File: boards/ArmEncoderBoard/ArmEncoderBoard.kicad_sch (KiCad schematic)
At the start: 5 parts, among them J1 S6B-PH-SM4-TB

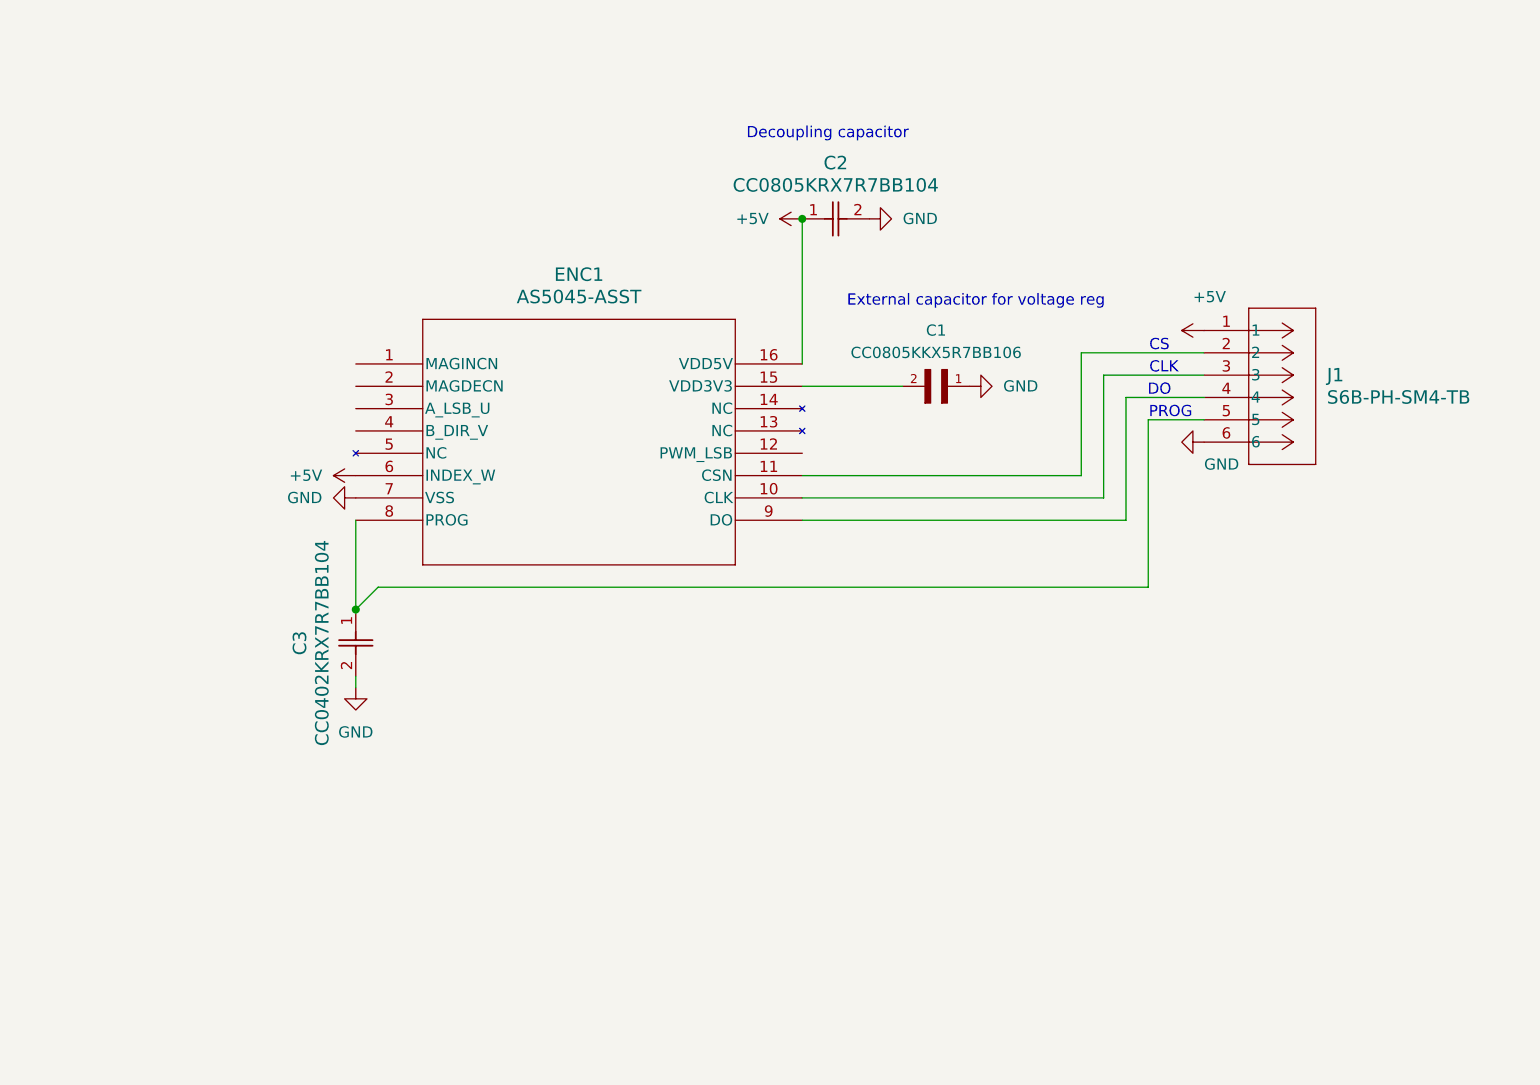
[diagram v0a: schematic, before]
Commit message: Footprints for encoder board dependencies
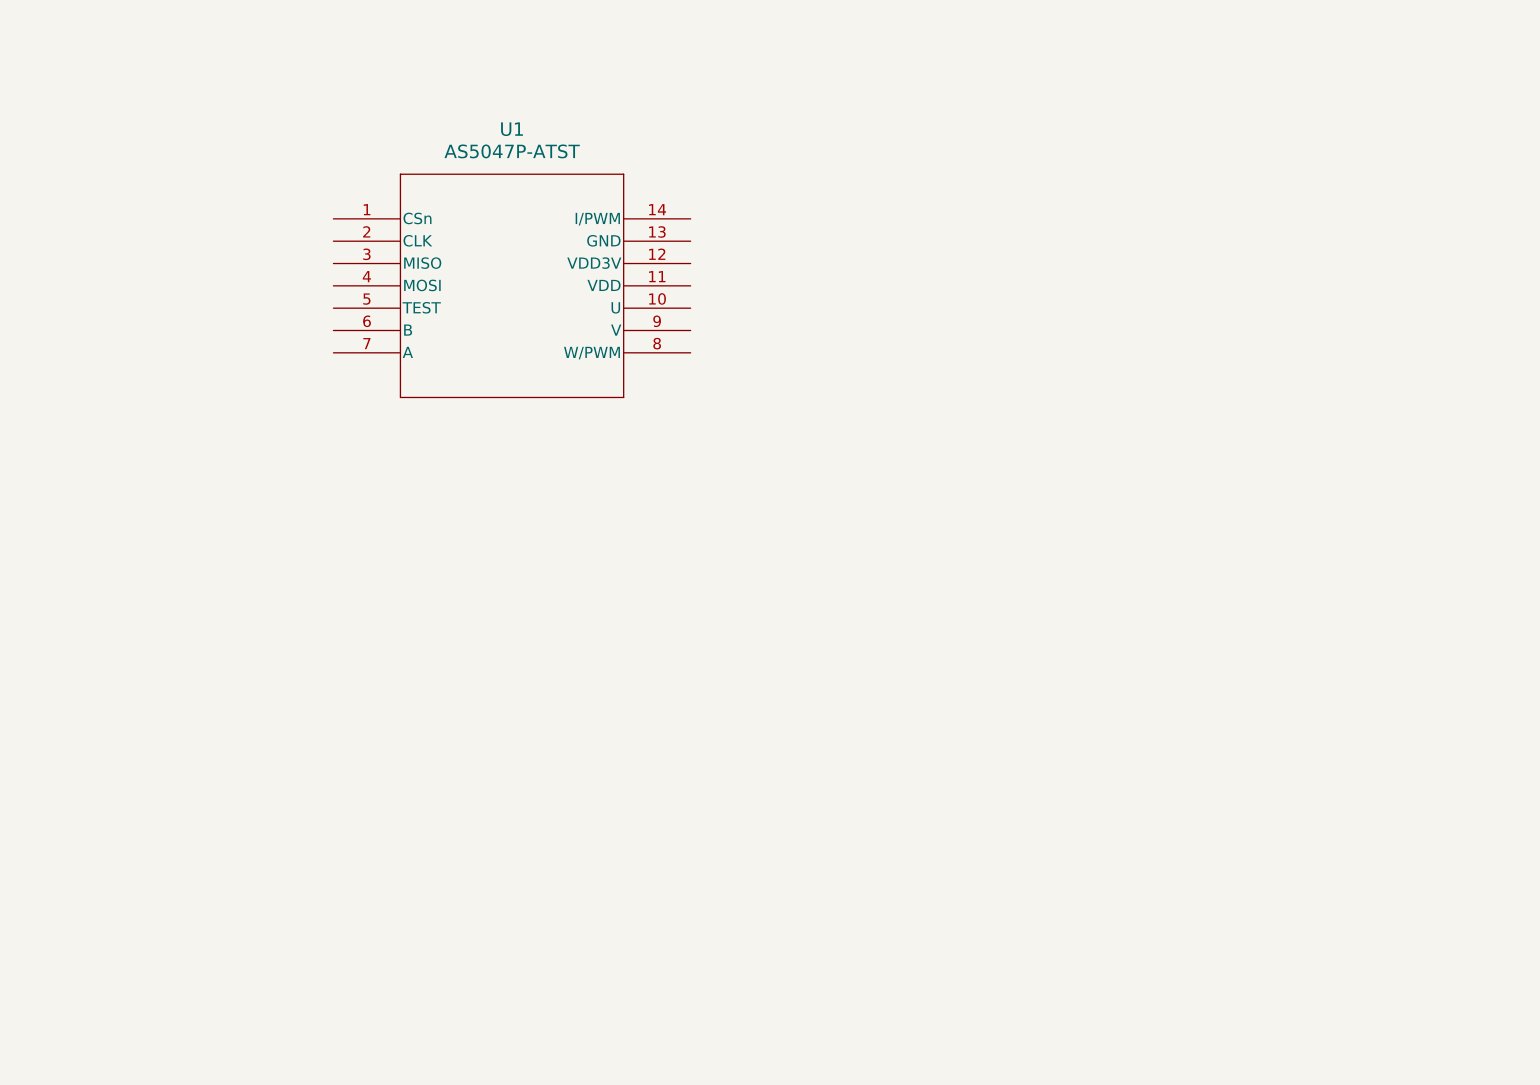
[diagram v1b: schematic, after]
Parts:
- removed C1: CC0805KKX5R7BB106, AS5045-3V3-REG-CAP:CAPC2012X70, symbol AS5045-3V-REG:CC0805KKX5R7BB106
- removed C2: CC0805KRX7R7BB104, CC0805N_YAG, symbol AS5045-DECOUPL-CAP:CC0805KRX7R7BB104
- removed C3: CC0402KRX7R7BB104, YAG_CC0402_YAG, symbol AS5045-PROG-CAP:CC0402KRX7R7BB104
- removed ENC1: AS5045-ASST, SSOP16_AS5040-ASST_AMS, symbol AS5045:AS5040-ASST
- removed J1: S6B-PH-SM4-TB, CONN_S6B-XH-SM4-TB_JST, symbol JST-XH-6:S6B-XH-SM4-TB
- added U1: AS5047P-ATST, AS5047P:AS5047P-ATST, symbol AS5047P:AS5047P-ATSM
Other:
- note removed: "CLK"
- note removed: "CS"
- note removed: "DO"
- note removed: "Decoupling capacitor"
- note removed: "External capacitor for voltage reg"
- note removed: "PROG"

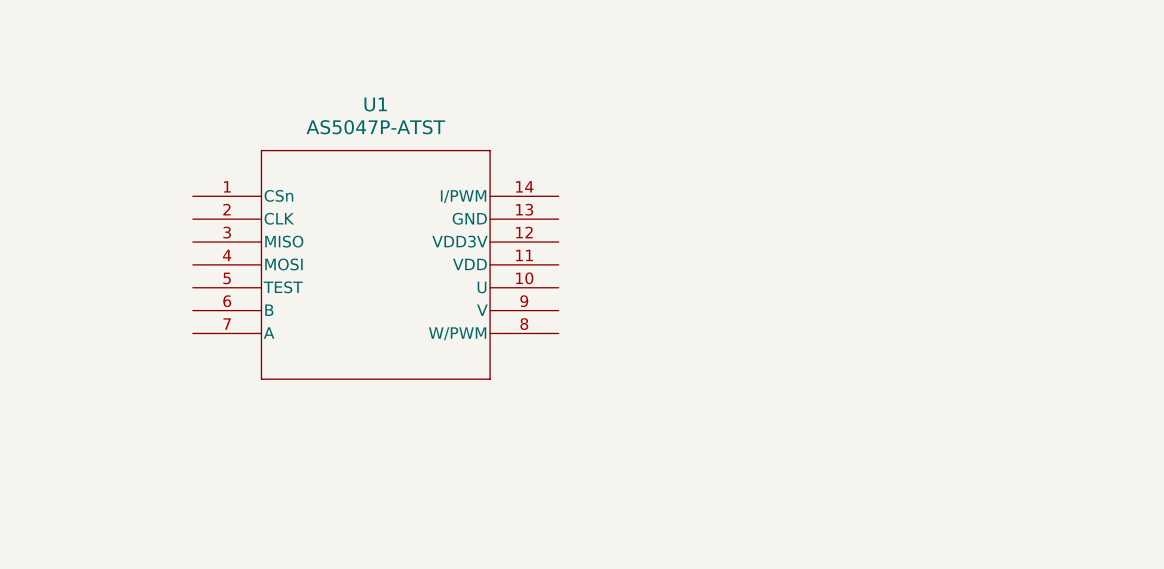
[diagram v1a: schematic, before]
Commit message: Split into leg and arm, finish arm encoder
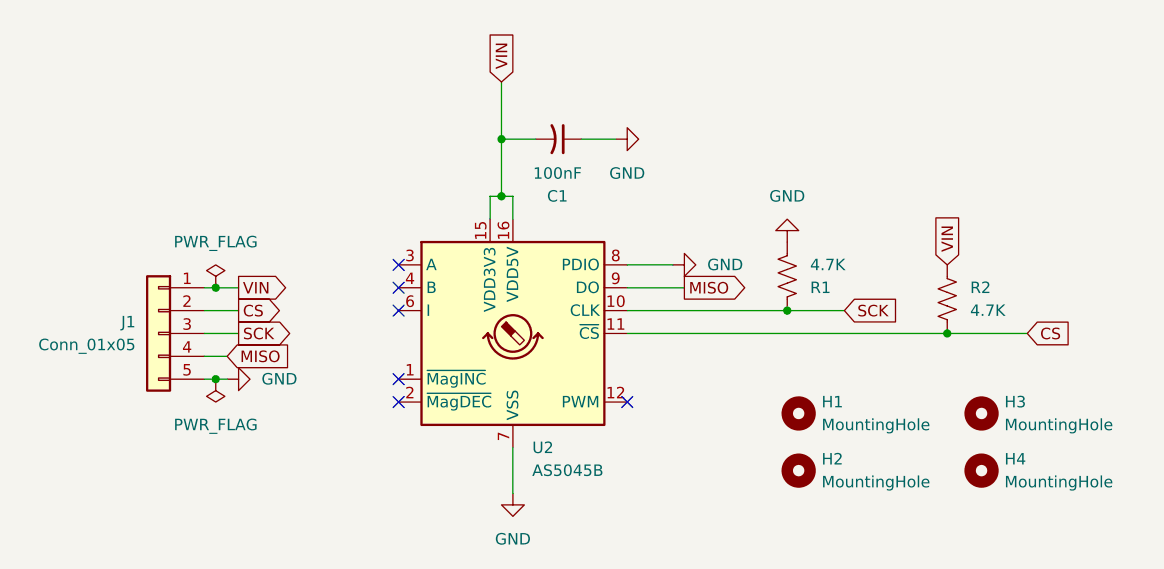
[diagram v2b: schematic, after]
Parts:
- removed U1: AS5047P-ATST, AS5047P:AS5047P-ATST, symbol AS5047P:AS5047P-ATSM
- added C1: 100nF, Capacitor100nF:885342208002, symbol Device:C_Small_US
- added H1, H2, H3, H4: MountingHole, MountingHole:MountingHole_3.5mm_Pad, symbol Mechanical:MountingHole
- added J1: Conn_01x05, Connector_JST:JST_XH_B5B-XH-A_1x05_P2.50mm_Vertical, symbol Connector_Generic:Conn_01x05
- added R1, R2: 4.7K, Resistor4.7K:CR0603-FX-4701ELF, symbol Device:R_US
- added U2: AS5045B, Package_SO:SSOP-16_5.3x6.2mm_P0.65mm, symbol Sensor_Magnetic:AS5045B
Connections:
- new net CS: J1.2 (Pin_2), R2.2, U2.11 (~{CS})
- new net GND: C1.1, J1.5 (Pin_5), R1.2, U2.7 (VSS), U2.8 (PDIO)
- new net MISO: J1.4 (Pin_4), U2.9 (DO)
- new net SCK: J1.3 (Pin_3), R1.1, U2.10 (CLK)
- new net VIN: C1.2, J1.1 (Pin_1), R2.1, U2.15 (VDD3V3), U2.16 (VDD5V)
- no-connect marks 0 -> 6
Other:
- title: Upper Arm Encoder Board -> Arm Encoder Board

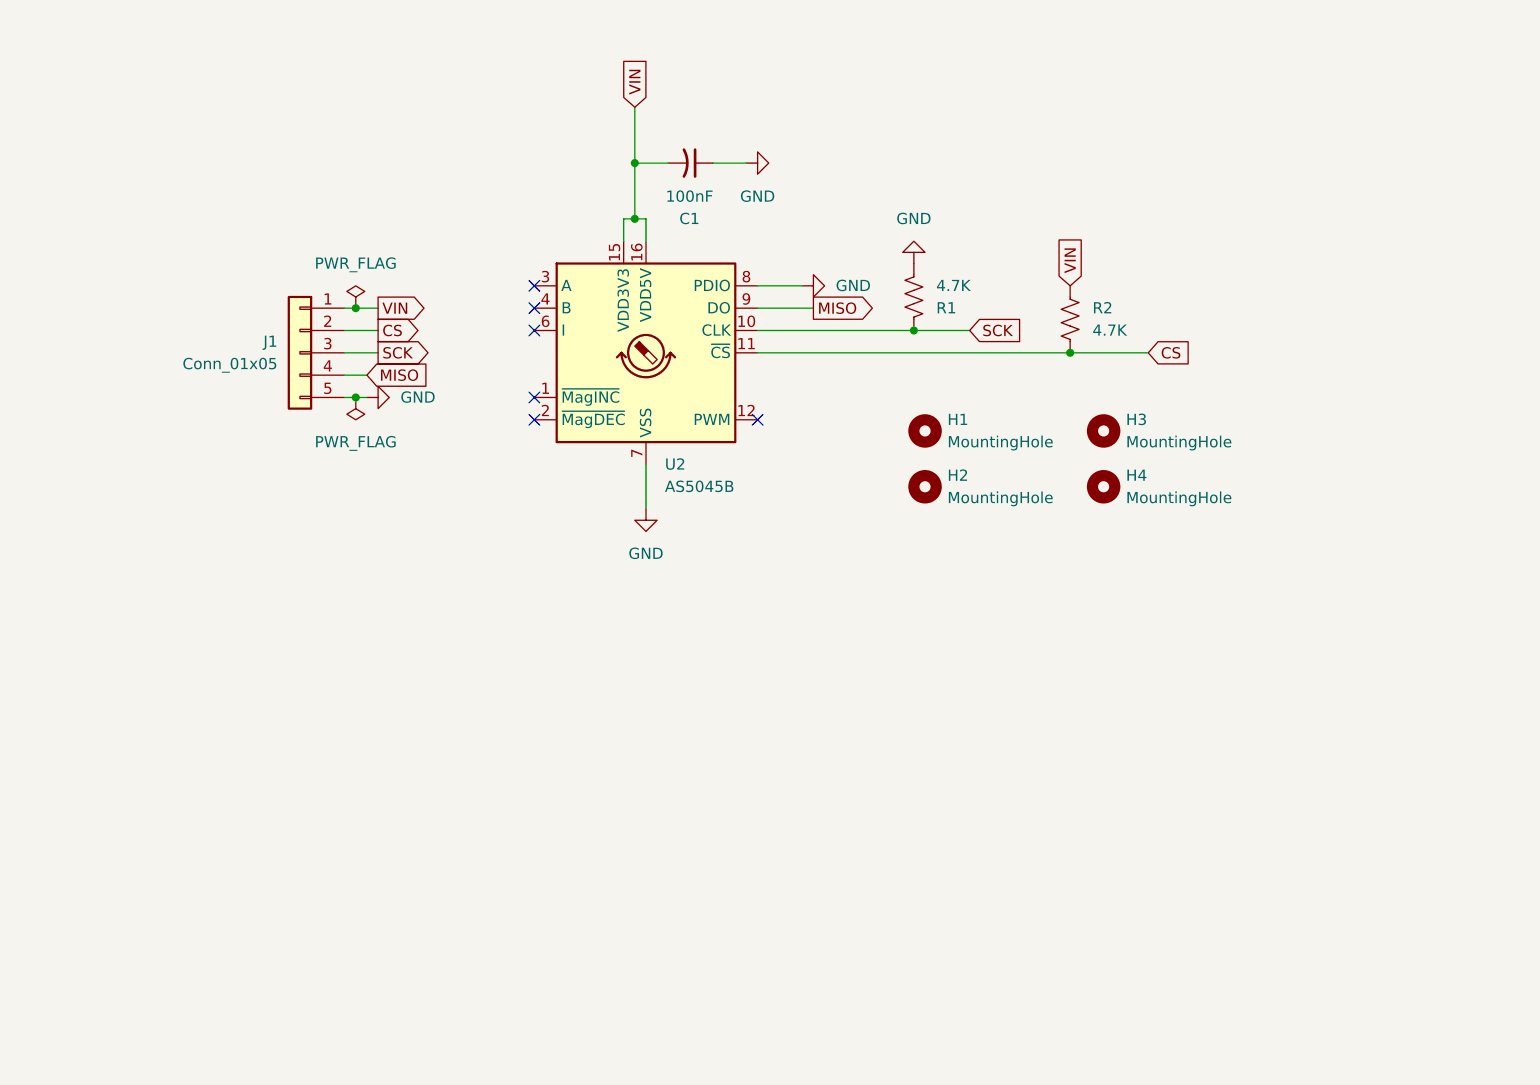
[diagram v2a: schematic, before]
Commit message: Arm encoder initial bom update
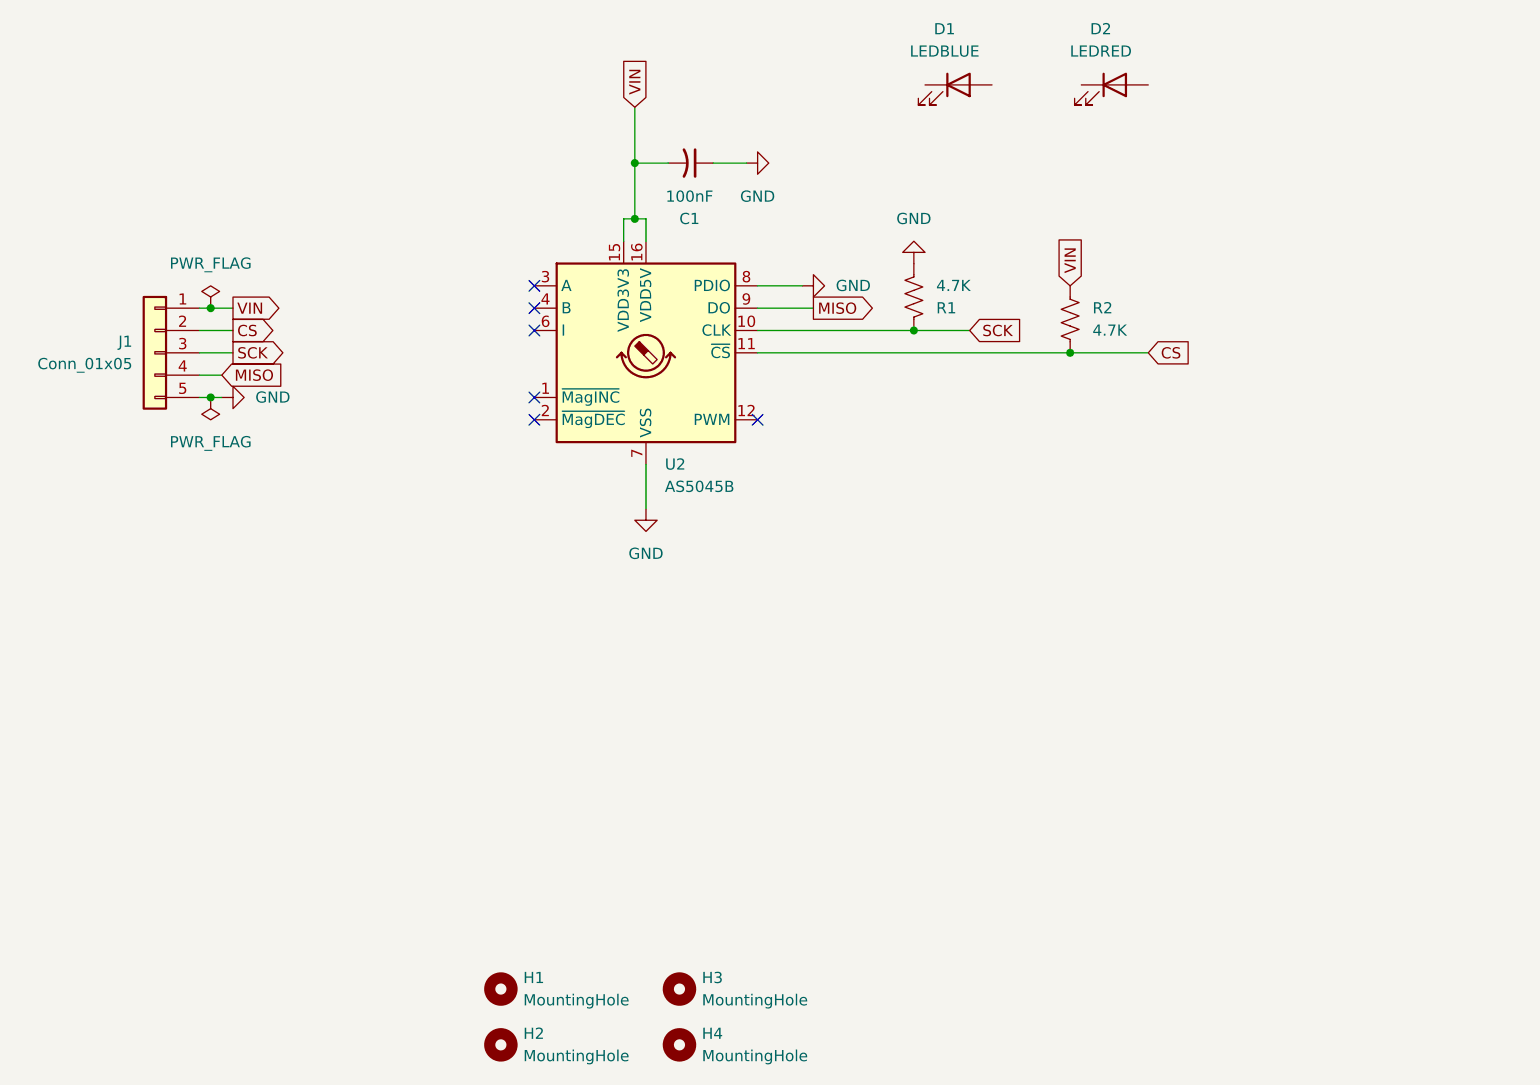
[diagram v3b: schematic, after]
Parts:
- added D1: LEDBLUE, LedBlue:YLED0603B, symbol Device:LED
- added D2: LEDRED, LedRed:YLED0603R, symbol Device:LED
- C1: footprint Capacitor100nF:885342208002 -> Capacitor100nF:CC0603KRX7R9BB104
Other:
- moved on the sheet: H1, H2, H3, H4, J1
